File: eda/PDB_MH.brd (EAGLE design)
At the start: 101.6 x 81.3 mm, 18 parts

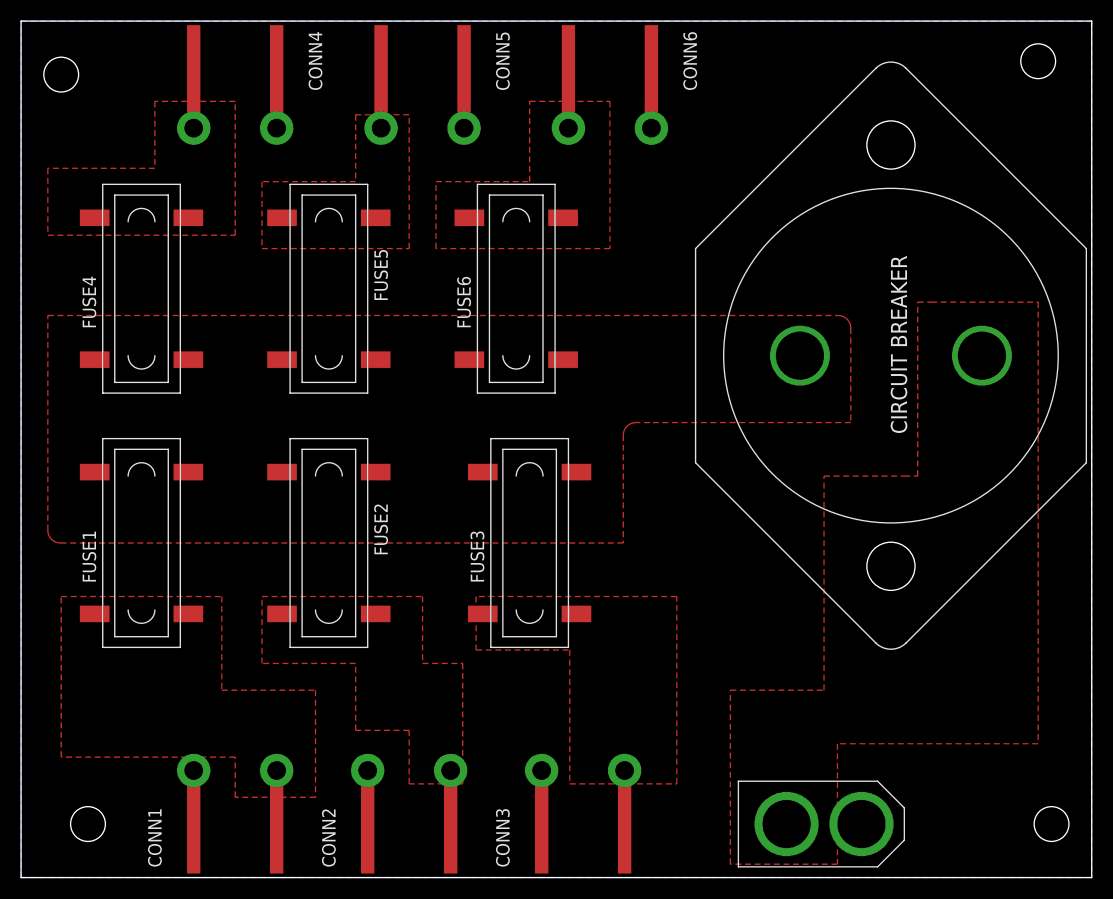
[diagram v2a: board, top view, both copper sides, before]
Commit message: Change names, broaden polygons, remove thermals, reformat sch
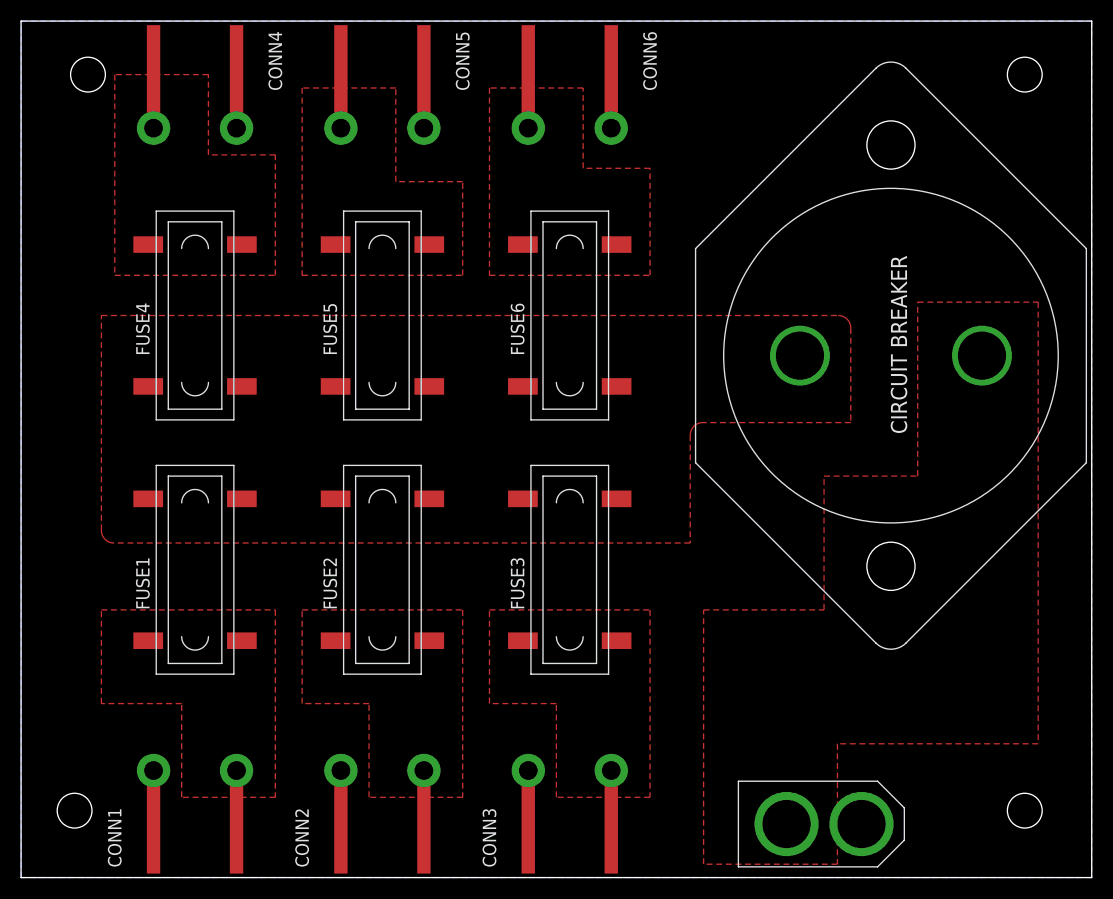
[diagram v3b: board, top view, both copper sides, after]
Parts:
- moved FUSE1 5.68 mm to (16.5, 29.2)
- moved FUSE4 5.68 mm to (16.5, 53.3)
- moved FUSE2 5.68 mm to (34.3, 29.2), turned to 90 degrees
- moved FUSE5 5.68 mm to (34.3, 53.3), turned to 90 degrees
- moved FUSE6 5.68 mm to (52.1, 53.3)
- moved FUSE3 4.58 mm to (52.1, 29.2)
- moved CONN5 3.81 mm to (34.3, 71.1)
- moved CONN6 3.81 mm to (52.1, 71.1)
- moved CONN1 3.81 mm to (16.5, 10.2)
- moved CONN4 3.81 mm to (16.5, 71.1)
- moved U$5 2.84 mm to (95.2, 6.35)
- moved U$3 2.54 mm to (6.35, 76.2)
- moved CONN2 2.54 mm to (34.3, 10.2)
- moved U$2 1.80 mm to (5.08, 6.35)
- moved U$4 1.80 mm to (95.2, 76.2)
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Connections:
- net 12V: now also FUSE2.P$2_DOWN, FUSE2.P$2_UP, FUSE5.P$1_DOWN, FUSE5.P$1_UP; no longer FUSE2.P$1_DOWN, FUSE2.P$1_UP, FUSE5.P$2_DOWN, FUSE5.P$2_UP
- net VOUT2: now also FUSE2.P$1_DOWN, FUSE2.P$1_UP; no longer FUSE2.P$2_DOWN, FUSE2.P$2_UP
- net VOUT5: now also FUSE5.P$2_DOWN, FUSE5.P$2_UP; no longer FUSE5.P$1_DOWN, FUSE5.P$1_UP

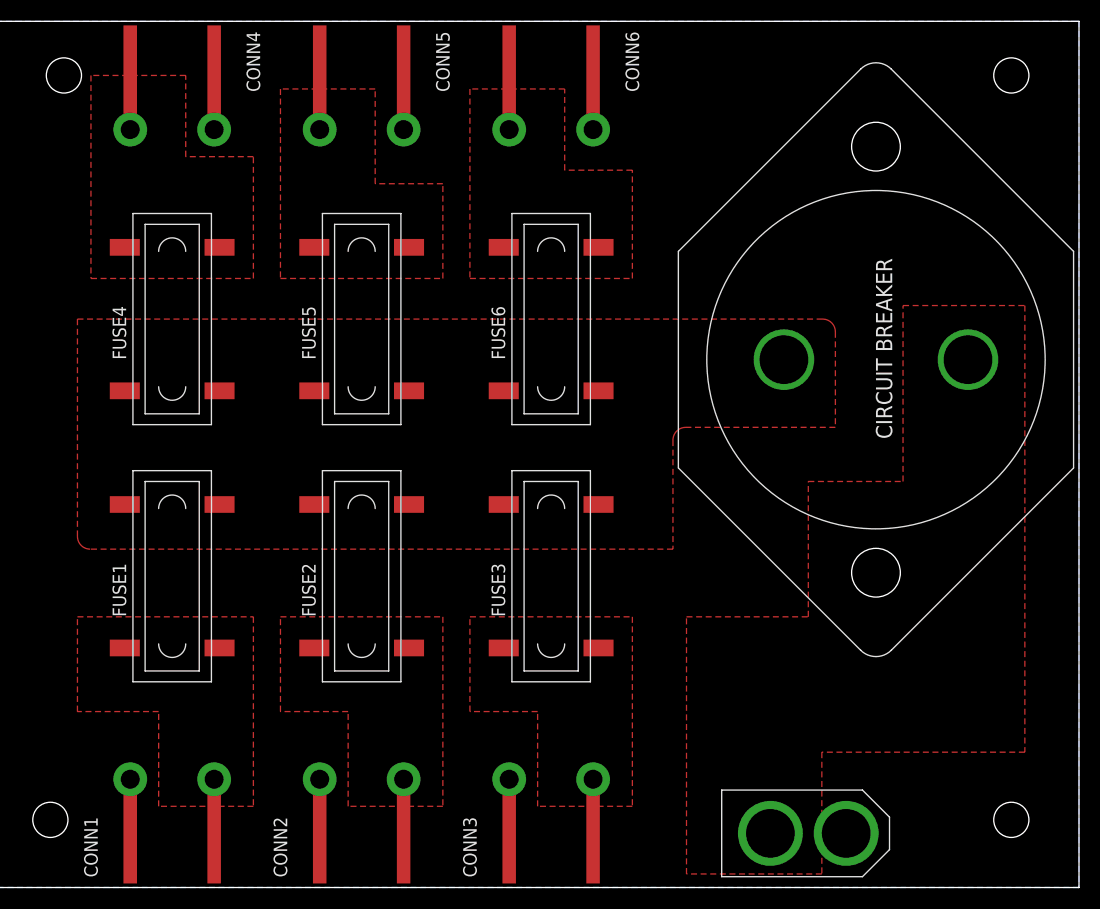
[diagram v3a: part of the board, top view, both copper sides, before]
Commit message: Made Polygons out of the planes. Established Plane priority. Turned on Thermals. Altered Position of XT60 Switch.
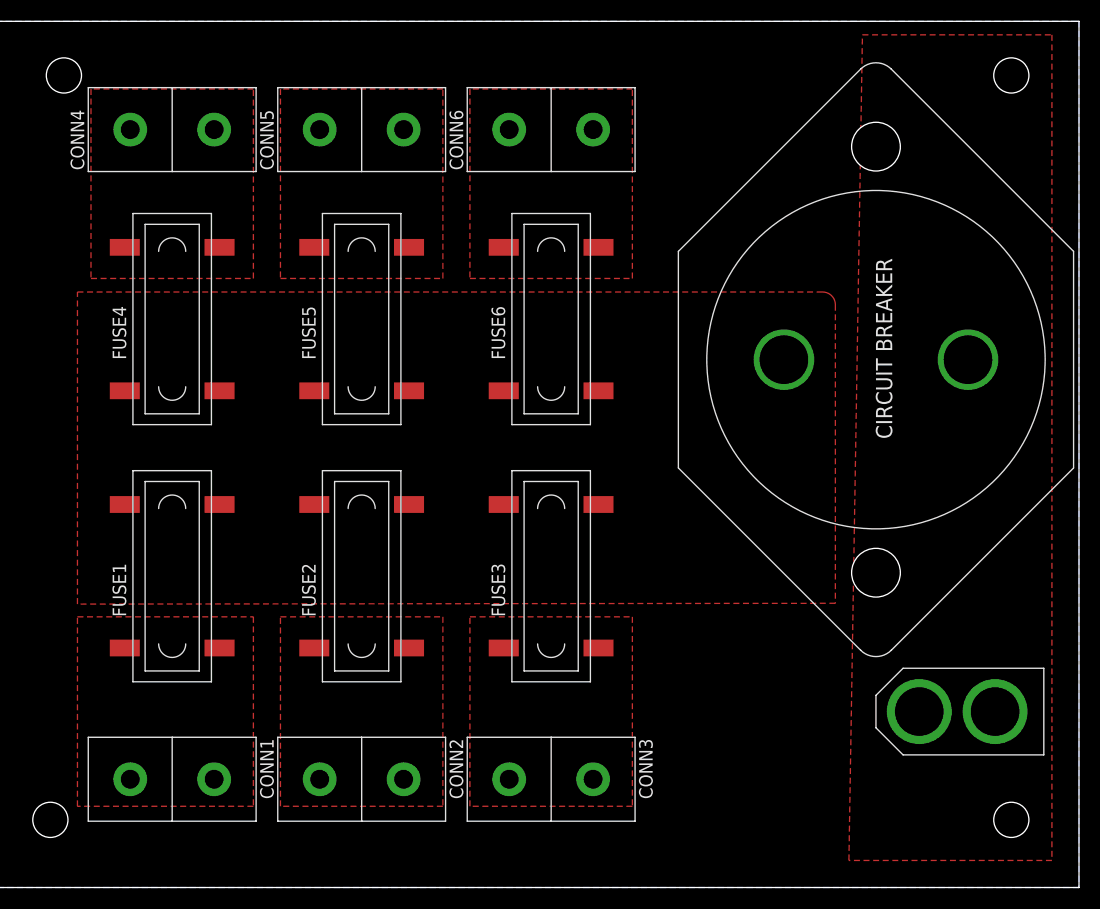
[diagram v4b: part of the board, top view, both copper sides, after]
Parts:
- CONN1, CONN2, CONN3, CONN4, CONN5, CONN6: value ANDERSONHORIZONTAL -> ANDERSONVERTICAL; device pie:ANDERSON_HORIZONTAL -> pie:ANDERSON_VERTICAL
- moved U$1 18.1 mm to (90.2, 16.5), turned to 180 degrees
- turned CONN1 to 270 degrees
- turned CONN2 to 270 degrees
- turned CONN3 to 270 degrees
- turned CONN4 to 90 degrees
- turned CONN5 to 90 degrees
- turned CONN6 to 90 degrees
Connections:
- net GND: no longer CONN1.PIN1-LEAD, CONN2.PIN1-LEAD, CONN3.PIN1-LEAD, CONN4.PIN1-LEAD, CONN5.PIN1-LEAD, CONN6.PIN1-LEAD
- net VOUT1: no longer CONN1.PIN2-LEAD
- net VOUT2: no longer CONN2.PIN2-LEAD
- net VOUT3: no longer CONN3.PIN2-LEAD
- net VOUT4: no longer CONN4.PIN2-LEAD
- net VOUT5: no longer CONN5.PIN2-LEAD
- net VOUT6: no longer CONN6.PIN2-LEAD
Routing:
- net GND: track 32.0 -> 0.00 mm
- net VOUT3: track 5.33 -> 0.00 mm
- net VOUT2: track 5.33 -> 0.00 mm
- net VOUT1: track 5.33 -> 0.00 mm
- net VOUT6: track 5.33 -> 0.00 mm
- net VOUT5: track 5.33 -> 0.00 mm
- net VOUT4: track 5.33 -> 0.00 mm
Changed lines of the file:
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@@
 </autorouter>
 <elements>
-<element name="CONN3" library="pie" package="ANDERSON_HORIZONTAL" value="ANDERSONHORIZONTAL" x="52.07" y="10.16" rot="R90">
-<attribute name="PIE-INT-REF-NUM" value="Anderson" x="52.07" y="10.16" size="1.778" layer="27" rot="R90" display="off"/>
+<element name="CONN3" library="pie" package="ANDERSON_VERTICAL" value="ANDERSONVERTICAL" x="52.07" y="10.16" rot="R270">
+<attribute name="PIE-INT-REF-NUM" value="Anderson" x="52.07" y="10.16" size="1.778" layer="27" rot="R270" display="off"/>
 </element>
-<element name="CONN1" library="pie" package="ANDERSON_HORIZONTAL" value="ANDERSONHORIZONTAL" x="16.51" y="10.16" rot="R90">
-<attribute name="PIE-INT-REF-NUM" value="Anderson" x="16.51" y="10.16" size="1.778" layer="27" rot="R90" display="off"/>
+<element name="CONN1" library="pie" package="ANDERSON_VERTICAL" value="ANDERSONVERTICAL" x="16.51" y="10.16" rot="R270">
+<attribute name="PIE-INT-REF-NUM" value="Anderson" x="16.51" y="10.16" size="1.778" layer="27" rot="R270" display="off"/>
 </element>
-<element name="CONN2" library="pie" package="ANDERSON_HORIZONTAL" value="ANDERSONHORIZONTAL" x="34.29" y="10.16" rot="R90">
-<attribute name="PIE-INT-REF-NUM" value="Anderson" x="34.29" y="10.16" size="1.778" layer="27" rot="R90" display="off"/>
+<element name="CONN2" library="pie" package="ANDERSON_VERTICAL" value="ANDERSONVERTICAL" x="34.29" y="10.16" rot="R270">
+<attribute name="PIE-INT-REF-NUM" value="Anderson" x="34.29" y="10.16" size="1.778" layer="27" rot="R270" display="off"/>
 </element>
-<element name="CONN4" library="pie" package="ANDERSON_HORIZONTAL" value="ANDERSONHORIZONTAL" x="16.51" y="71.12" rot="R270">
-<attribute name="PIE-INT-REF-NUM" value="Anderson" x="16.51" y="71.12" size="1.778" layer="27" rot="R270" display="off"/>
+<element name="CONN4" library="pie" package="ANDERSON_VERTICAL" value="ANDERSONVERTICAL" x="16.51" y="71.12" rot="R90">
+<attribute name="PIE-INT-REF-NUM" value="Anderson" x="16.51" y="71.12" size="1.778" layer="27" rot="R90" display="off"/>
 </element>
-<element name="U$1" library="pie" package="XT60CONNECTOR" value="XT60CONNECTOR" x="76.2" y="5.08">
-<attribute name="PARTNUMBER" value="PRT-10474 " x="76.2" y="5.08" size="1.778" layer="27" display="off"/>
+<element name="U$1" library="pie" package="XT60CONNECTOR" value="XT60CONNECTOR" x="90.17" y="16.51" rot="R180">
+<attribute name="PARTNUMBER" value="PRT-10474 " x="90.17" y="16.51" size="1.778" layer="27" rot="R180" display="off"/>
 </element>
 <element name="CIRCUIT_BREAKER" library="pie" package="CIRC_BREAKER" value="CIRC_BREAKER" x="82.55" y="49.53" rot="R270">
@@
 <attribute name="MANUF-PN" value="3587" x="52.07" y="53.34" size="1.778" layer="27" rot="R90" display="off"/>
 </element>
-<element name="CONN5" library="pie" package="ANDERSON_HORIZONTAL" value="ANDERSONHORIZONTAL" x="34.29" y="71.12" rot="R270">
-<attribute name="PIE-INT-REF-NUM" value="Anderson" x="34.29" y="71.12" size="1.778" layer="27" rot="R270" display="off"/>
+<element name="CONN5" library="pie" package="ANDERSON_VERTICAL" value="ANDERSONVERTICAL" x="34.29" y="71.12" rot="R90">
+<attribute name="PIE-INT-REF-NUM" value="Anderson" x="34.29" y="71.12" size="1.778" layer="27" rot="R90" display="off"/>
 </element>
-<element name="CONN6" library="pie" package="ANDERSON_HORIZONTAL" value="ANDERSONHORIZONTAL" x="52.07" y="71.12" rot="R270">
-<attribute name="PIE-INT-REF-NUM" value="Anderson" x="52.07" y="71.12" size="1.778" layer="27" rot="R270" display="off"/>
+<element name="CONN6" library="pie" package="ANDERSON_VERTICAL" value="ANDERSONVERTICAL" x="52.07" y="71.12" rot="R90">
+<attribute name="PIE-INT-REF-NUM" value="Anderson" x="52.07" y="71.12" size="1.778" layer="27" rot="R90" display="off"/>
 </element>
 <element name="U$2" library="pie" package="STAND-OFF" value="" x="5.08" y="6.35"/>
@@
 <signals>
 <signal name="GND">
-<polygon width="1.1938" layer="16">
+<polygon width="1.1938" layer="16" rank="6">
 <vertex x="0" y="81.28"/>
 <vertex x="101.6" y="81.28"/>
@@
 <contactref element="U$1" pad="GND"/>
 <contactref element="CONN1" pad="PIN1"/>
-<contactref element="CONN1" pad="PIN1-LEAD"/>
 <contactref element="CONN2" pad="PIN1"/>
-<contactref element="CONN2" pad="PIN1-LEAD"/>
-<wire x1="30.353" y1="10.16" x2="30.353" y2="4.826" width="0.4064" layer="1"/>
 <contactref element="CONN3" pad="PIN1"/>
-<contactref element="CONN3" pad="PIN1-LEAD"/>
 <contactref element="CONN4" pad="PIN1"/>
-<contactref element="CONN4" pad="PIN1-LEAD"/>
 <contactref element="CONN5" pad="PIN1"/>
-<contactref element="CONN5" pad="PIN1-LEAD"/>
 <contactref element="CONN6" pad="PIN1"/>
-<contactref element="CONN6" pad="PIN1-LEAD"/>
-<wire x1="56.007" y1="71.12" x2="56.007" y2="76.454" width="0.4064" layer="1"/>
-<wire x1="12.573" y1="10.16" x2="12.573" y2="4.826" width="0.4064" layer="1"/>
-<wire x1="20.447" y1="71.12" x2="20.447" y2="76.454" width="0.4064" layer="1"/>
-<wire x1="38.227" y1="71.12" x2="38.227" y2="76.454" width="0.4064" layer="1"/>
-<wire x1="48.133" y1="10.16" x2="48.133" y2="4.826" width="0.4064" layer="1"/>
 </signal>
 <signal name="VOUT2">
@@
 <contactref element="FUSE2" pad="P$1_DOWN"/>
 <contactref element="CONN2" pad="PIN2"/>
-<contactref element="CONN2" pad="PIN2-LEAD"/>
-<wire x1="38.227" y1="10.16" x2="38.227" y2="4.826" width="0.4064" layer="1"/>
-<polygon width="1.1938" layer="1">
+<polygon width="1.1938" layer="1" isolate="1.27">
 <vertex x="26.67" y="25.4"/>
 <vertex x="41.91" y="25.4"/>
 <vertex x="41.91" y="7.62"/>
-<vertex x="33.02" y="7.62"/>
-<vertex x="33.02" y="16.51"/>
-<vertex x="26.67" y="16.51"/>
+<vertex x="26.67" y="7.62"/>
 </polygon>
 </signal>
 <signal name="VOUT1">
 <contactref element="CONN1" pad="PIN2"/>
-<contactref element="CONN1" pad="PIN2-LEAD"/>
 <contactref element="FUSE1" pad="P$1_UP"/>
 <contactref element="FUSE1" pad="P$1_DOWN"/>
-<wire x1="20.447" y1="10.16" x2="20.447" y2="4.826" width="0.4064" layer="1"/>
-<polygon width="1.1938" layer="1">
+<polygon width="1.1938" layer="1" isolate="1.27">
 <vertex x="7.62" y="25.4"/>
 <vertex x="24.13" y="25.4"/>
 <vertex x="24.13" y="7.62"/>
-<vertex x="15.24" y="7.62"/>
-<vertex x="15.24" y="16.51"/>
-<vertex x="7.62" y="16.51"/>
+<vertex x="7.62" y="7.62"/>
 </polygon>
 </signal>
 <signal name="VOUT3">
 <contactref element="CONN3" pad="PIN2"/>
-<contactref element="CONN3" pad="PIN2-LEAD"/>
 <contactref element="FUSE3" pad="P$1_UP"/>
 <contactref element="FUSE3" pad="P$1_DOWN"/>
-<wire x1="56.007" y1="10.16" x2="56.007" y2="4.826" width="0.4064" layer="1"/>
-<polygon width="1.1938" layer="1">
+<polygon width="1.1938" layer="1" isolate="1.27">
 <vertex x="44.45" y="25.4"/>
 <vertex x="59.69" y="25.4"/>
 <vertex x="59.69" y="7.62"/>
-<vertex x="50.8" y="7.62"/>
-<vertex x="50.8" y="16.51"/>
-<vertex x="44.45" y="16.51"/>
+<vertex x="44.45" y="7.62"/>
 </polygon>
 </signal>
@@
 <contactref element="FUSE4" pad="P$2_DOWN"/>
 <contactref element="CONN4" pad="PIN2"/>
-<contactref element="CONN4" pad="PIN2-LEAD"/>
-<wire x1="12.573" y1="71.12" x2="12.573" y2="76.454" width="0.4064" layer="1"/>
-<polygon width="1.1938" layer="1" thermals="no">
+<polygon width="1.1938" layer="1" isolate="1.27">
 <vertex x="8.89" y="57.15"/>
 <vertex x="24.13" y="57.15"/>
-<vertex x="24.13" y="68.58"/>
-<vertex x="17.78" y="68.58"/>
-<vertex x="17.78" y="76.2"/>
-<vertex x="8.89" y="76.2"/>
+<vertex x="24.13" y="74.93"/>
+<vertex x="8.89" y="74.93"/>
 </polygon>
 </signal>
@@
 <contactref element="FUSE5" pad="P$2_UP"/>
 <contactref element="FUSE5" pad="P$2_DOWN"/>
-<contactref element="CONN5" pad="PIN2-LEAD"/>
 <contactref element="CONN5" pad="PIN2"/>
-<wire x1="30.353" y1="71.12" x2="30.353" y2="76.454" width="0.4064" layer="1"/>
-<polygon width="1.1938" layer="1" thermals="no">
+<polygon width="1.1938" layer="1" isolate="1.27">
 <vertex x="26.67" y="57.15"/>
 <vertex x="41.91" y="57.15"/>
-<vertex x="41.91" y="66.04"/>
-<vertex x="35.56" y="66.04"/>
-<vertex x="35.56" y="74.93"/>
+<vertex x="41.91" y="74.93"/>
 <vertex x="26.67" y="74.93"/>
 </polygon>
@@
 <contactref element="FUSE5" pad="P$1_UP"/>
 <contactref element="FUSE5" pad="P$1_DOWN"/>
-<polygon width="1.1938" layer="1" thermals="no">
-<vertex x="7.62" y="53.34"/>
-<vertex x="77.5462" y="53.34" curve="-90"/>
-<vertex x="78.74" y="52.1462"/>
-<vertex x="78.74" y="43.18"/>
-<vertex x="64.6938" y="43.18" curve="90"/>
-<vertex x="63.5" y="41.9862"/>
-<vertex x="63.5" y="31.75"/>
-<vertex x="8.8138" y="31.75" curve="-90"/>
-<vertex x="7.62" y="32.9438"/>
+<polygon width="1.1938" layer="1" isolate="1.27" rank="2">
+<vertex x="7.62" y="55.88"/>
+<vertex x="77.5462" y="55.88" curve="-90"/>
+<vertex x="78.74" y="54.6862"/>
+<vertex x="78.74" y="26.67"/>
+<vertex x="7.62" y="26.5938"/>
 </polygon>
 <contactref element="FUSE1" pad="P$2_UP"/>
@@
 <contactref element="CIRCUIT_BREAKER" pad="P$1"/>
 <contactref element="U$1" pad="12V"/>
-<polygon width="1.1938" layer="1">
-<vertex x="85.09" y="54.61"/>
-<vertex x="96.52" y="54.61"/>
-<vertex x="96.52" y="12.7"/>
-<vertex x="77.47" y="12.7"/>
-<vertex x="77.47" y="1.27"/>
-<vertex x="64.77" y="1.27"/>
-<vertex x="64.77" y="25.4"/>
-<vertex x="76.2" y="25.4"/>
-<vertex x="76.2" y="38.1"/>
-<vertex x="85.09" y="38.1"/>
+<polygon width="1.1938" layer="1" isolate="1.27" rank="3">
+<vertex x="81.28" y="80.01"/>
+<vertex x="99.06" y="80.01"/>
+<vertex x="99.06" y="2.54"/>
+<vertex x="80.01" y="2.54"/>
 </polygon>
 </signal>
@@
 <contactref element="FUSE6" pad="P$2_DOWN"/>
 <contactref element="CONN6" pad="PIN2"/>
-<contactref element="CONN6" pad="PIN2-LEAD"/>
-<wire x1="48.133" y1="71.12" x2="48.133" y2="76.454" width="0.4064" layer="1"/>
-<polygon width="1.1938" layer="1" thermals="no">
+<polygon width="1.1938" layer="1" isolate="1.27">
 <vertex x="44.45" y="57.15"/>
 <vertex x="59.69" y="57.15"/>
-<vertex x="59.69" y="67.31"/>
-<vertex x="53.34" y="67.31"/>
-<vertex x="53.34" y="74.93"/>
+<vertex x="59.69" y="74.93"/>
 <vertex x="44.45" y="74.93"/>
 </polygon>
